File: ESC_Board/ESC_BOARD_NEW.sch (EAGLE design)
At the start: 165 parts, among them J3 AVR_SPI_PROG_3X2NS, U2 ATMEGA328P_TQFP, U4 PCA9685

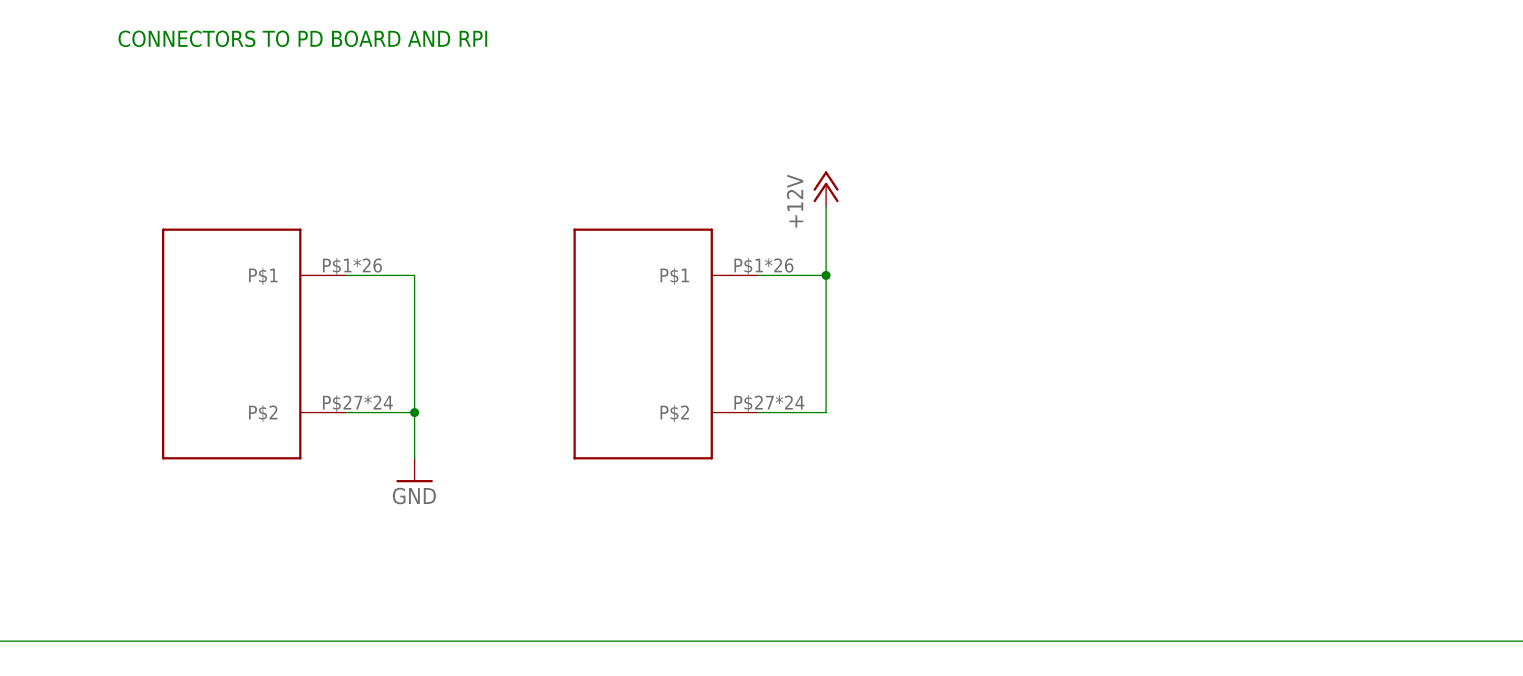
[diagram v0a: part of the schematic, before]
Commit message: Added standard ESC to power distribution board connector
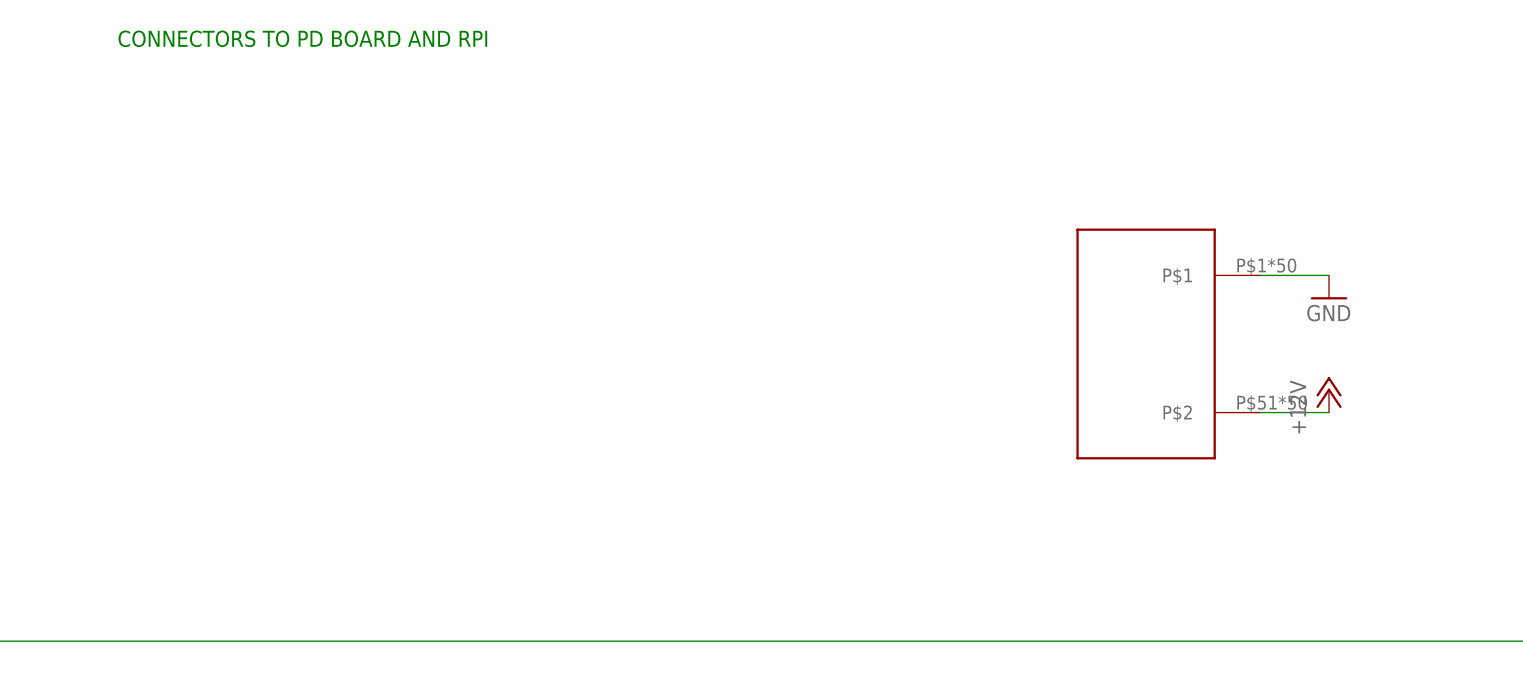
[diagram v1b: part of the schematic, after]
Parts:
- removed U$17, U$18: POWER-BRICK-CONNECTOR, MotherboardParts:POWER-BRICK-CONNECTOR
- added U$14: ESC-CONNECTORESC-CONNECTOR, MotherboardParts:ESC-CONNECTORESC-CONNECTOR
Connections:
- net +12V: now also U$14.P$2; no longer U$18.P$1, U$18.P$2
- net GND: now also U$14.P$1; no longer U$17.P$1, U$17.P$2
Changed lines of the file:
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@@
 <?xml version="1.0" encoding="utf-8"?>
 <!DOCTYPE eagle SYSTEM "eagle.dtd">
-<eagle version="8.4.3">
+<eagle version="8.5.0">
 <drawing>
 <settings>
@@
 <part name="GND94" library="SparkFun-PowerSymbols" deviceset="GND" device=""/>
 <part name="GND95" library="SparkFun-PowerSymbols" deviceset="GND" device=""/>
-<part name="U$17" library="MotherboardParts" deviceset="POWER-BRICK-CONNECTOR" device=""/>
-<part name="U$18" library="MotherboardParts" deviceset="POWER-BRICK-CONNECTOR" device=""/>
 <part name="U$16" library="MotherBoardParts2" deviceset="POWER_BRICK_CONNECTORS(2X6)" device=""/>
 <part name="GND" library="supply1" deviceset="GND" device=""/>
@@
 <part name="GND71" library="supply1" library_urn="urn:adsk.eagle:library:371" deviceset="GND" device=""/>
 <part name="GND72" library="supply1" library_urn="urn:adsk.eagle:library:371" deviceset="GND" device=""/>
+<part name="U$14" library="MotherboardParts" deviceset="ESC-CONNECTOR" device="ESC-CONNECTOR"/>
 </parts>
 <sheets>
@@
 <instance part="GND94" gate="1" x="-157.48" y="106.68"/>
 <instance part="GND95" gate="1" x="-144.78" y="106.68"/>
-<instance part="U$17" gate="G$1" x="312.42" y="403.86"/>
-<instance part="U$18" gate="G$1" x="358.14" y="403.86"/>
 <instance part="U$16" gate="G$1" x="248.92" y="406.4"/>
 <instance part="GND" gate="1" x="220.98" y="403.86"/>
 <instance part="FRAME5" gate="G$1" x="185.42" y="246.38"/>
 <instance part="P+32" gate="1" x="274.32" y="419.1"/>
-<instance part="P+34" gate="1" x="378.46" y="421.64"/>
-<instance part="GND96" gate="1" x="332.74" y="388.62"/>
+<instance part="P+34" gate="1" x="434.34" y="398.78"/>
+<instance part="GND96" gate="1" x="434.34" y="408.94"/>
 <instance part="P1" gate="G$1" x="99.06" y="408.94" rot="MR0"/>
 <instance part="P2" gate="G$1" x="86.36" y="406.4" rot="MR0"/>
@@
 <instance part="GND71" gate="1" x="396.24" y="119.38"/>
 <instance part="GND72" gate="1" x="340.36" y="119.38"/>
+<instance part="U$14" gate="G$1" x="414.02" y="403.86"/>
 </instances>
 <busses>
@@
 </segment>
 <segment>
-<pinref part="U$17" gate="G$1" pin="P$2"/>
-<pinref part="GND96" gate="1" pin="GND"/>
-<wire x1="325.12" y1="396.24" x2="332.74" y2="396.24" width="0.1524" layer="91"/>
-<wire x1="332.74" y1="396.24" x2="332.74" y2="391.16" width="0.1524" layer="91"/>
-<pinref part="U$17" gate="G$1" pin="P$1"/>
-<wire x1="325.12" y1="411.48" x2="332.74" y2="411.48" width="0.1524" layer="91"/>
-<wire x1="332.74" y1="411.48" x2="332.74" y2="396.24" width="0.1524" layer="91"/>
-<junction x="332.74" y="396.24"/>
-</segment>
-<segment>
 <pinref part="C70" gate="G$1" pin="2"/>
 <wire x1="241.3" y1="208.28" x2="241.3" y2="205.74" width="0.1524" layer="91"/>
@@
 <wire x1="396.24" y1="121.92" x2="396.24" y2="124.46" width="0.1524" layer="91"/>
 </segment>
+<segment>
+<pinref part="U$14" gate="G$1" pin="P$1"/>
+<wire x1="426.72" y1="411.48" x2="434.34" y2="411.48" width="0.1524" layer="91"/>
+<pinref part="GND96" gate="1" pin="GND"/>
+</segment>
 </net>
 <net name="+12V" class="0">
@@
 </segment>
 <segment>
-<pinref part="P+34" gate="1" pin="+12V"/>
-<pinref part="U$18" gate="G$1" pin="P$1"/>
-<wire x1="370.84" y1="411.48" x2="378.46" y2="411.48" width="0.1524" layer="91"/>
-<wire x1="378.46" y1="411.48" x2="378.46" y2="419.1" width="0.1524" layer="91"/>
-<pinref part="U$18" gate="G$1" pin="P$2"/>
-<wire x1="370.84" y1="396.24" x2="378.46" y2="396.24" width="0.1524" layer="91"/>
-<wire x1="378.46" y1="396.24" x2="378.46" y2="411.48" width="0.1524" layer="91"/>
-<junction x="378.46" y="411.48"/>
-</segment>
-<segment>
 <pinref part="P+2" gate="1" pin="+12V"/>
 <pinref part="F1" gate="G$1" pin="2"/>
@@
 <wire x1="274.32" y1="408.94" x2="274.32" y2="416.56" width="0.1524" layer="91"/>
 </segment>
+<segment>
+<pinref part="U$14" gate="G$1" pin="P$2"/>
+<wire x1="426.72" y1="396.24" x2="434.34" y2="396.24" width="0.1524" layer="91"/>
+<pinref part="P+34" gate="1" pin="+12V"/>
+</segment>
 </net>

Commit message: Some final changes
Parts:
- U$14: value ESC-CONNECTORESC-CONNECTOR -> ESC-CONNECTORPARALLELL; device MotherboardParts:ESC-CONNECTORESC-CONNECTOR -> MotherboardParts:ESC-CONNECTORPARALLELL
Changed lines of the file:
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@@
 <grid distance="0.1" unitdist="inch" unit="inch" style="lines" multiple="1" display="no" altdistance="0.01" altunitdist="inch" altunit="inch"/>
 <layers>
-<layer number="1" name="Top" color="4" fill="1" visible="no" active="no"/>
-<layer number="2" name="Route2" color="1" fill="3" visible="no" active="no"/>
-<layer number="3" name="Route3" color="4" fill="3" visible="no" active="no"/>
-<layer number="4" name="Route4" color="1" fill="4" visible="no" active="no"/>
-<layer number="5" name="Route5" color="4" fill="4" visible="no" active="no"/>
-<layer number="6" name="Route6" color="1" fill="8" visible="no" active="no"/>
-<layer number="7" name="Route7" color="4" fill="8" visible="no" active="no"/>
-<layer number="8" name="Route8" color="1" fill="2" visible="no" active="no"/>
-<layer number="9" name="Route9" color="4" fill="2" visible="no" active="no"/>
-<layer number="10" name="Route10" color="1" fill="7" visible="no" active="no"/>
-<layer number="11" name="Route11" color="4" fill="7" visible="no" active="no"/>
-<layer number="12" name="Route12" color="1" fill="5" visible="no" active="no"/>
-<layer number="13" name="Route13" color="4" fill="5" visible="no" active="no"/>
-<layer number="14" name="Route14" color="1" fill="6" visible="no" active="no"/>
-<layer number="15" name="Route15" color="4" fill="6" visible="no" active="no"/>
-<layer number="16" name="Bottom" color="1" fill="1" visible="no" active="no"/>
-<layer number="17" name="Pads" color="2" fill="1" visible="no" active="no"/>
-<layer number="18" name="Vias" color="2" fill="1" visible="no" active="no"/>
-<layer number="19" name="Unrouted" color="6" fill="1" visible="no" active="no"/>
-<layer number="20" name="Dimension" color="24" fill="1" visible="no" active="no"/>
-<layer number="21" name="tPlace" color="7" fill="1" visible="no" active="no"/>
-<layer number="22" name="bPlace" color="7" fill="1" visible="no" active="no"/>
-<layer number="23" name="tOrigins" color="15" fill="1" visible="no" active="no"/>
-<layer number="24" name="bOrigins" color="15" fill="1" visible="no" active="no"/>
-<layer number="25" name="tNames" color="7" fill="1" visible="no" active="no"/>
-<layer number="26" name="bNames" color="7" fill="1" visible="no" active="no"/>
-<layer number="27" name="tValues" color="7" fill="1" visible="no" active="no"/>
-<layer number="28" name="bValues" color="7" fill="1" visible="no" active="no"/>
+<layer number="1" name="Top" color="4" fill="1" visible="yes" active="no"/>
+<layer number="2" name="Route2" color="1" fill="3" visible="yes" active="no"/>
+<layer number="3" name="Route3" color="4" fill="3" visible="yes" active="no"/>
+<layer number="4" name="Route4" color="1" fill="4" visible="yes" active="no"/>
+<layer number="5" name="Route5" color="4" fill="4" visible="yes" active="no"/>
+<layer number="6" name="Route6" color="1" fill="8" visible="yes" active="no"/>
+<layer number="7" name="Route7" color="4" fill="8" visible="yes" active="no"/>
+<layer number="8" name="Route8" color="1" fill="2" visible="yes" active="no"/>
+<layer number="9" name="Route9" color="4" fill="2" visible="yes" active="no"/>
+<layer number="10" name="Route10" color="1" fill="7" visible="yes" active="no"/>
+<layer number="11" name="Route11" color="4" fill="7" visible="yes" active="no"/>
+<layer number="12" name="Route12" color="1" fill="5" visible="yes" active="no"/>
+<layer number="13" name="Route13" color="4" fill="5" visible="yes" active="no"/>
+<layer number="14" name="Route14" color="1" fill="6" visible="yes" active="no"/>
+<layer number="15" name="Route15" color="4" fill="6" visible="yes" active="no"/>
+<layer number="16" name="Bottom" color="1" fill="1" visible="yes" active="no"/>
+<layer number="17" name="Pads" color="2" fill="1" visible="yes" active="no"/>
+<layer number="18" name="Vias" color="2" fill="1" visible="yes" active="no"/>
+<layer number="19" name="Unrouted" color="6" fill="1" visible="yes" active="no"/>
+<layer number="20" name="Dimension" color="24" fill="1" visible="yes" active="no"/>
+<layer number="21" name="tPlace" color="7" fill="1" visible="yes" active="no"/>
+<layer number="22" name="bPlace" color="7" fill="1" visible="yes" active="no"/>
+<layer number="23" name="tOrigins" color="15" fill="1" visible="yes" active="no"/>
+<layer number="24" name="bOrigins" color="15" fill="1" visible="yes" active="no"/>
+<layer number="25" name="tNames" color="7" fill="1" visible="yes" active="no"/>
+<layer number="26" name="bNames" color="7" fill="1" visible="yes" active="no"/>
+<layer number="27" name="tValues" color="7" fill="1" visible="yes" active="no"/>
+<layer number="28" name="bValues" color="7" fill="1" visible="yes" active="no"/>
 <layer number="29" name="tStop" color="7" fill="3" visible="no" active="no"/>
 <layer number="30" name="bStop" color="7" fill="6" visible="no" active="no"/>
@@
 <layer number="35" name="tGlue" color="7" fill="4" visible="no" active="no"/>
 <layer number="36" name="bGlue" color="7" fill="5" visible="no" active="no"/>
-<layer number="37" name="tTest" color="7" fill="1" visible="no" active="no"/>
-<layer number="38" name="bTest" color="7" fill="1" visible="no" active="no"/>
+<layer number="37" name="tTest" color="7" fill="1" visible="yes" active="no"/>
+<layer number="38" name="bTest" color="7" fill="1" visible="yes" active="no"/>
 <layer number="39" name="tKeepout" color="4" fill="11" visible="no" active="no"/>
 <layer number="40" name="bKeepout" color="1" fill="11" visible="no" active="no"/>
@@
 <layer number="44" name="Drills" color="7" fill="1" visible="no" active="no"/>
 <layer number="45" name="Holes" color="7" fill="1" visible="no" active="no"/>
-<layer number="46" name="Milling" color="3" fill="1" visible="no" active="no"/>
-<layer number="47" name="Measures" color="7" fill="1" visible="no" active="no"/>
-<layer number="48" name="Document" color="7" fill="1" visible="no" active="no"/>
-<layer number="49" name="Reference" color="7" fill="1" visible="no" active="no"/>
-<layer number="50" name="dxf" color="7" fill="1" visible="no" active="no"/>
-<layer number="51" name="tDocu" color="7" fill="1" visible="no" active="no"/>
-<layer number="52" name="bDocu" color="7" fill="1" visible="no" active="no"/>
-<layer number="53" name="tGND_GNDA" color="7" fill="9" visible="no" active="no"/>
-<layer number="54" name="bGND_GNDA" color="1" fill="9" visible="no" active="no"/>
-<layer number="56" name="wert" color="7" fill="1" visible="no" active="no"/>
-<layer number="57" name="tCAD" color="7" fill="1" visible="no" active="no"/>
-<layer number="59" name="tCarbon" color="7" fill="1" visible="no" active="no"/>
-<layer number="60" name="bCarbon" color="7" fill="1" visible="no" active="no"/>
+<layer number="46" name="Milling" color="3" fill="1" visible="yes" active="no"/>
+<layer number="47" name="Measures" color="7" fill="1" visible="yes" active="no"/>
+<layer number="48" name="Document" color="7" fill="1" visible="yes" active="no"/>
+<layer number="49" name="Reference" color="7" fill="1" visible="yes" active="no"/>
+<layer number="50" name="dxf" color="7" fill="1" visible="yes" active="no"/>
+<layer number="51" name="tDocu" color="7" fill="1" visible="yes" active="no"/>
+<layer number="52" name="bDocu" color="7" fill="1" visible="yes" active="no"/>
+<layer number="53" name="tGND_GNDA" color="7" fill="9" visible="yes" active="no"/>
+<layer number="54" name="bGND_GNDA" color="1" fill="9" visible="yes" active="no"/>
+<layer number="56" name="wert" color="7" fill="1" visible="yes" active="no"/>
+<layer number="57" name="tCAD" color="7" fill="1" visible="yes" active="no"/>
+<layer number="59" name="tCarbon" color="7" fill="1" visible="yes" active="no"/>
+<layer number="60" name="bCarbon" color="7" fill="1" visible="yes" active="no"/>
 <layer number="90" name="Modules" color="5" fill="1" visible="yes" active="yes"/>
 <layer number="91" name="Nets" color="2" fill="1" visible="yes" active="yes"/>
@@
 <part name="GND71" library="supply1" library_urn="urn:adsk.eagle:library:371" deviceset="GND" device=""/>
 <part name="GND72" library="supply1" library_urn="urn:adsk.eagle:library:371" deviceset="GND" device=""/>
-<part name="U$14" library="MotherboardParts" deviceset="ESC-CONNECTOR" device="ESC-CONNECTOR"/>
+<part name="U$14" library="MotherboardParts" deviceset="ESC-CONNECTOR" device="PARALLELL" value="ESC-CONNECTORPARALLELL"/>
 </parts>
 <sheets>

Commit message: Added way to power electro magnets
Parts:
- added J4, J6: (no value), SparkFun-Connectors:CONN_02
- added LED10, LED9: (no value), led:LEDSML0603
- added R4, R5: 330, resistor:R-US_R0603
- added U1, U3: FQB27P06, CamSensComponents:FQB27P06
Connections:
- removed net PWME1: P6.1, U4.PWM6
- removed net PWME2: P7.1, U4.PWM7
- new net E_MAG_1: J4.2, R5.2, U1.D2
- new net E_MAG_1_ON: P6.1, U1.G2, U4.PWM6
- new net E_MAG_2: J6.2, R4.2, U3.D2
- new net E_MAG_2_ON: P7.1, U3.G2, U4.PWM7
- new net N$51: LED9.A, R5.1
- new net N$64: LED10.A, R4.1
- net +12V: now also U1.S2, U3.S2
- net GND: now also J4.1, J6.1, LED10.C, LED9.C
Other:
- note added: "Elecro Magnet 2"
- note added: "Electro Mangnet 1"

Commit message: fixed up some of ground plane
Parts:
- removed C7, C8: 0.1uF, rcl:C-EUC0603
- removed J2: (no value), SparkFun-Connectors:CONN_02
- removed LED7, LED8: WS2812B5050, microbuilder:WS2812B5050
- removed P10, P8, P9: (no value), SparkFun-Connectors:M01PTH
- removed R20, R21: 10k, SparkFun-Resistors:470OHM1/10W1%(0603)
- added P13, P14, P15: (no value), SparkFun-Connectors:M01PTH
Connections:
- removed net OUT7: LED7.DO, LED8.DI
- removed net OUT8: LED8.DO
- net +5V: no longer C7.1, C8.1, LED7.VDD, LED8.VDD, R20.2, R21.2
- net E4: no longer J2.2
- net GND: no longer C7.2, C8.2, J2.1, LED7.GND, LED8.GND
- net LED1: now also U4.PWM8; no longer U4.PWM13
- net LED2: now also U4.PWM9; no longer U4.PWM14
- net OUT6: no longer LED7.DI
- net PIEZO: now also U4.PWM10; no longer U4.PWM15
- net PWM11: now also P15.1, U4.PWM15; no longer P12.1, U4.PWM12
- net PWM3: now also P12.1, U4.PWM12; no longer P9.1, U4.PWM9
- net PWM4: now also P11.1, U4.PWM11; no longer P8.1, U4.PWM8
- net PWM7: now also P14.1, U4.PWM14; no longer P11.1, U4.PWM11
- net PWM8: now also P13.1, U4.PWM13; no longer P10.1, U4.PWM10
- net SCL: no longer R21.1
- net SDA: no longer R20.1
